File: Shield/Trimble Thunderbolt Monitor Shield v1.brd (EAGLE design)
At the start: 160 x 100 mm, 32 parts, among them Q1 2N2222, U2 MAX232PTH

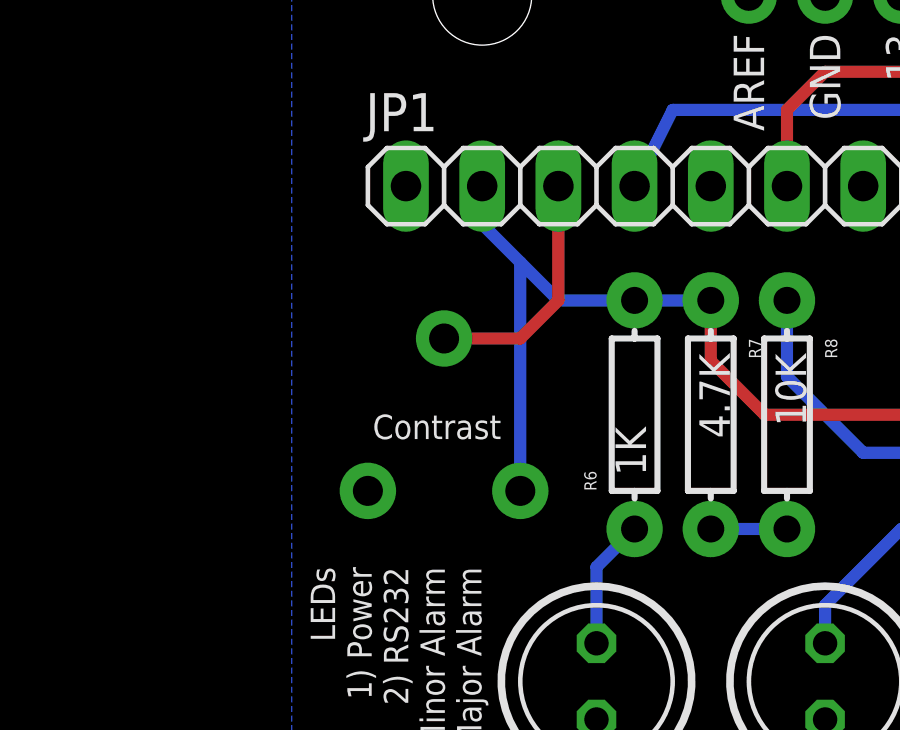
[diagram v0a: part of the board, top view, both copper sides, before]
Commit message: Changed the pot used for LCD contrast to a 3362U package.
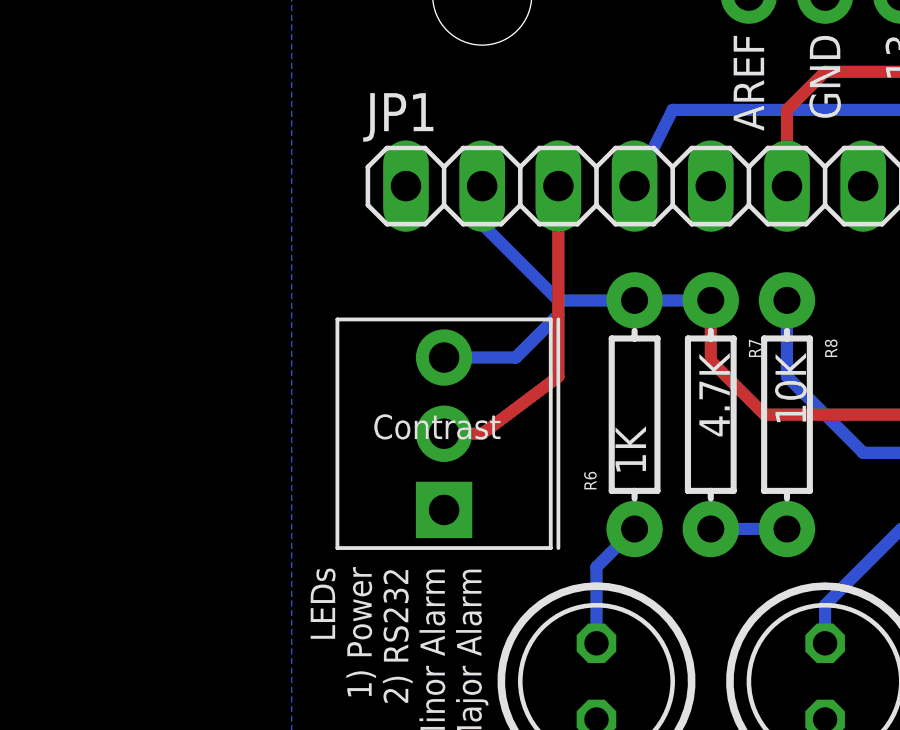
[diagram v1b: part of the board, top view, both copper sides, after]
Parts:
- TRIMLCD: device SparkFun:TRIM_POT -> SparkFun:3362U
- moved TRIMLCD 2.62 mm to (30.5, 73.0)
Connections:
- net +5V: now also TRIMLCD.P$3; no longer TRIMLCD.3
- net GND: now also TRIMLCD.P$1; no longer TRIMLCD.2
- net N$8: now also TRIMLCD.P$2; no longer TRIMLCD.1
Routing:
- net +5V: track 148.8 -> 146.0 mm
- net N$8: track 8.15 -> 10.8 mm
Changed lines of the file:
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@@
 </element>
 <element name="R6" library="SparkFun" package="AXIAL-0.3" value="1K" x="34.29" y="76.2" rot="R90"/>
-<element name="TRIMLCD" library="SparkFun" package="TRIM_POT" value="10K" x="27.94" y="73.66" rot="R90"/>
+<element name="TRIMLCD" library="SparkFun" package="3362U" value="10K" x="30.48" y="73.025" rot="R90"/>
 <element name="R7" library="SparkFun" package="AXIAL-0.3" value="4.7K" x="36.83" y="76.2" rot="R270"/>
 <element name="R8" library="SparkFun" package="AXIAL-0.3" value="10K" x="39.37" y="76.2" rot="R270"/>
@@
 <contactref element="S7" pad="2"/>
 <contactref element="LED1" pad="K"/>
-<contactref element="TRIMLCD" pad="2"/>
+<contactref element="TRIMLCD" pad="P$1"/>
 <contactref element="JP1" pad="1"/>
 <contactref element="Q1" pad="1"/>
@@
 <signal name="+5V">
 <contactref element="R6" pad="P$2"/>
-<contactref element="TRIMLCD" pad="3"/>
+<contactref element="TRIMLCD" pad="P$3"/>
 <contactref element="R7" pad="P$1"/>
 <contactref element="GND" pad="5V"/>
@@
 <wire x1="52.07" y1="43.18" x2="52.07" y2="41.91" width="0.4064" layer="1"/>
 <wire x1="29.21" y1="83.82" x2="29.21" y2="82.55" width="0.4064" layer="16"/>
-<wire x1="29.21" y1="82.55" x2="30.48" y2="81.28" width="0.4064" layer="16"/>
-<wire x1="30.48" y1="81.28" x2="31.75" y2="80.01" width="0.4064" layer="16"/>
+<wire x1="29.21" y1="82.55" x2="31.75" y2="80.01" width="0.4064" layer="16"/>
 <wire x1="31.75" y1="80.01" x2="34.29" y2="80.01" width="0.4064" layer="16"/>
 <wire x1="34.29" y1="80.01" x2="36.83" y2="80.01" width="0.4064" layer="16"/>
-<wire x1="30.48" y1="73.66" x2="30.48" y2="81.28" width="0.4064" layer="16"/>
 <wire x1="62.23" y1="83.82" x2="62.23" y2="86.36" width="0.4064" layer="16"/>
 <wire x1="62.23" y1="86.36" x2="63.5" y2="87.63" width="0.4064" layer="16"/>
@@
 <wire x1="78.74" y1="81.28" x2="77.47" y2="82.55" width="0.4064" layer="16"/>
 <wire x1="77.47" y1="82.55" x2="76.2" y2="82.55" width="0.4064" layer="16"/>
+<wire x1="27.94" y1="78.105" x2="30.330096875" y2="78.105" width="0.4064" layer="16"/>
+<wire x1="30.330096875" y1="78.105" x2="31.75" y2="79.524903125" width="0.4064" layer="16"/>
+<wire x1="31.75" y1="79.524903125" x2="31.75" y2="80.01" width="0.4064" layer="16"/>
 </signal>
 <signal name="N$8">
-<contactref element="TRIMLCD" pad="1"/>
+<contactref element="TRIMLCD" pad="P$2"/>
 <contactref element="JP1" pad="3"/>
-<wire x1="27.94" y1="78.74" x2="30.48" y2="78.74" width="0.4064" layer="1"/>
-<wire x1="30.48" y1="78.74" x2="31.75" y2="80.01" width="0.4064" layer="1"/>
-<wire x1="31.75" y1="80.01" x2="31.75" y2="83.82" width="0.4064" layer="1"/>
+<wire x1="31.75" y1="83.82" x2="31.75" y2="77.47" width="0.4064" layer="1"/>
+<wire x1="31.75" y1="77.47" x2="29.21" y2="75.565" width="0.4064" layer="1"/>
+<wire x1="29.21" y1="75.565" x2="27.94" y2="75.565" width="0.4064" layer="1"/>
 </signal>
 <signal name="N$11">

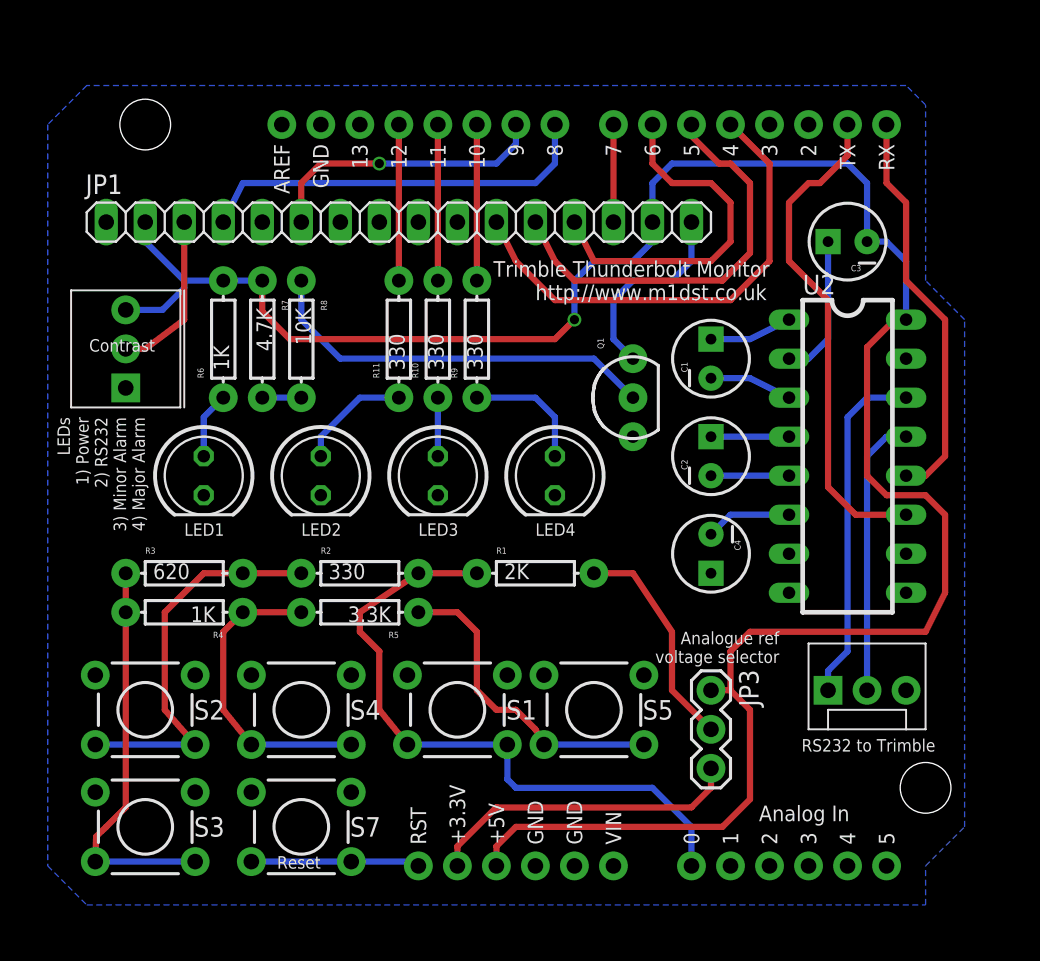
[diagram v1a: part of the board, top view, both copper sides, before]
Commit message: Backlight and track routing changes
Changes to the layout of some of the tracks to make them look neater.
Also changed the way the backlight interacts with the Netduino.  It is
now possible to control the brightness of the LCD via a pin on the
Netduino.

Also changed some of the LED output pins
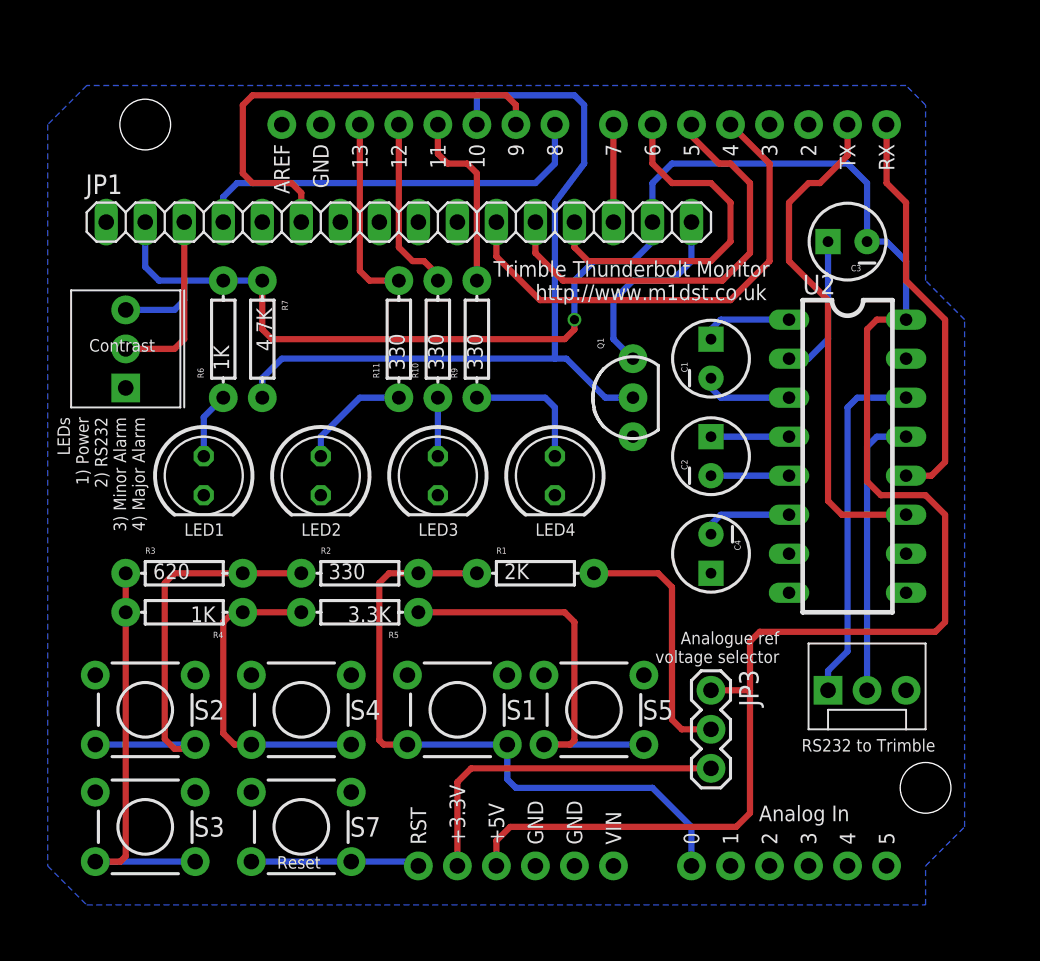
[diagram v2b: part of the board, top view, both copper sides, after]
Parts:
- removed R8: 10K, SparkFun:AXIAL-0.3
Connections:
- removed net N$11: R7.P$2, R8.P$2
- removed net N$12: Q1.2, R8.P$1
- new net D13: GND.D13, R11.P$2
- net D10: now also Q1.2, R7.P$2; no longer R9.P$2
- net D11: now also R9.P$2; no longer R10.P$2
- net D12: now also R10.P$2; no longer R11.P$2
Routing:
- net D10: track 10.2 -> 53.3 mm
- net N$12: track 26.2 -> 0.00 mm
- net D13: track 0.00 -> 12.3 mm
- net D9: track 18.8 -> 30.3 mm, vias 1 -> 0
- net N$5: track 20.6 -> 26.7 mm
- net +5V: track 146.0 -> 150.6 mm
- net N$11: track 2.54 -> 0.00 mm
- net N$20: track 25.8 -> 28.3 mm
- net N$19: track 14.5 -> 16.9 mm
- net D11: track 10.2 -> 12.0 mm
- net +3V3: track 20.6 -> 22.3 mm
- net D12: track 10.2 -> 11.6 mm
- net N$3: track 20.1 -> 21.2 mm
- net N$1: track 26.1 -> 27.0 mm
- net N$8: track 10.8 -> 11.7 mm
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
